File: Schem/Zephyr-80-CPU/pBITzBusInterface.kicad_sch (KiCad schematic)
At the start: 1 part, among them J1 pBITzBus

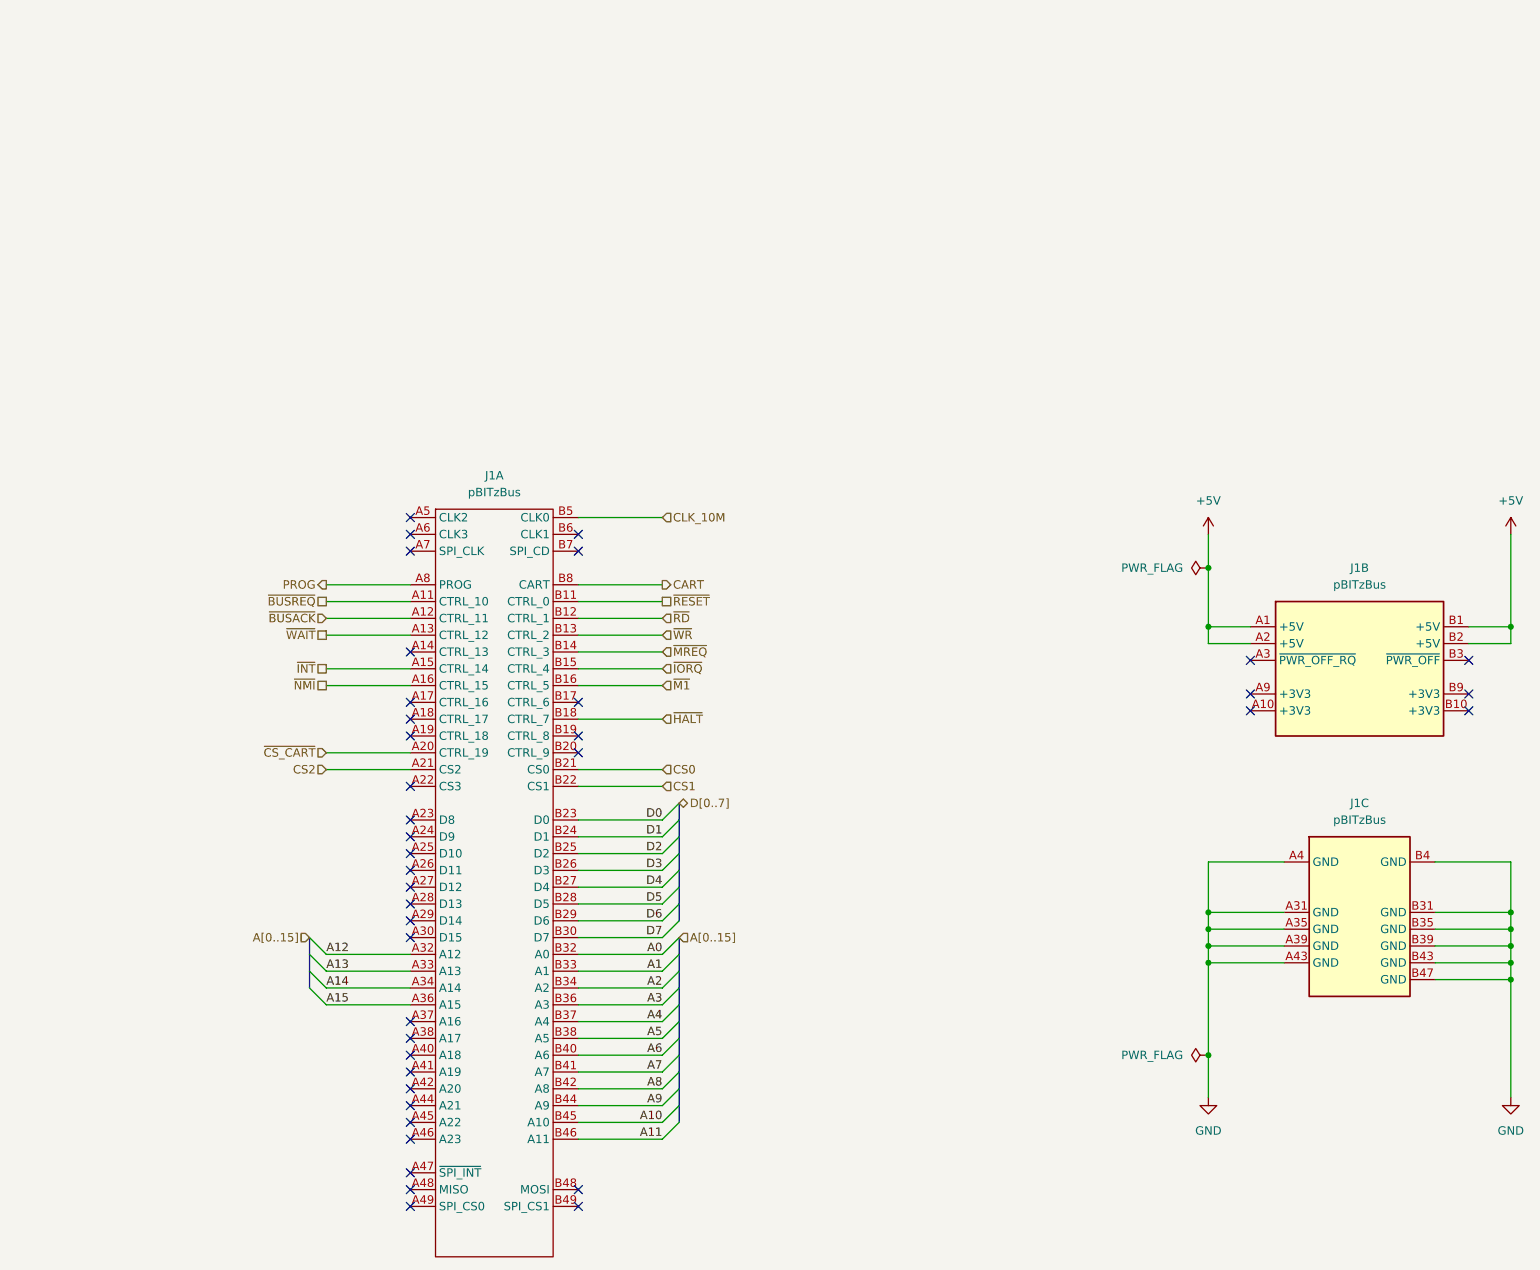
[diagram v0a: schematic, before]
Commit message: Moved to the DIN Connector
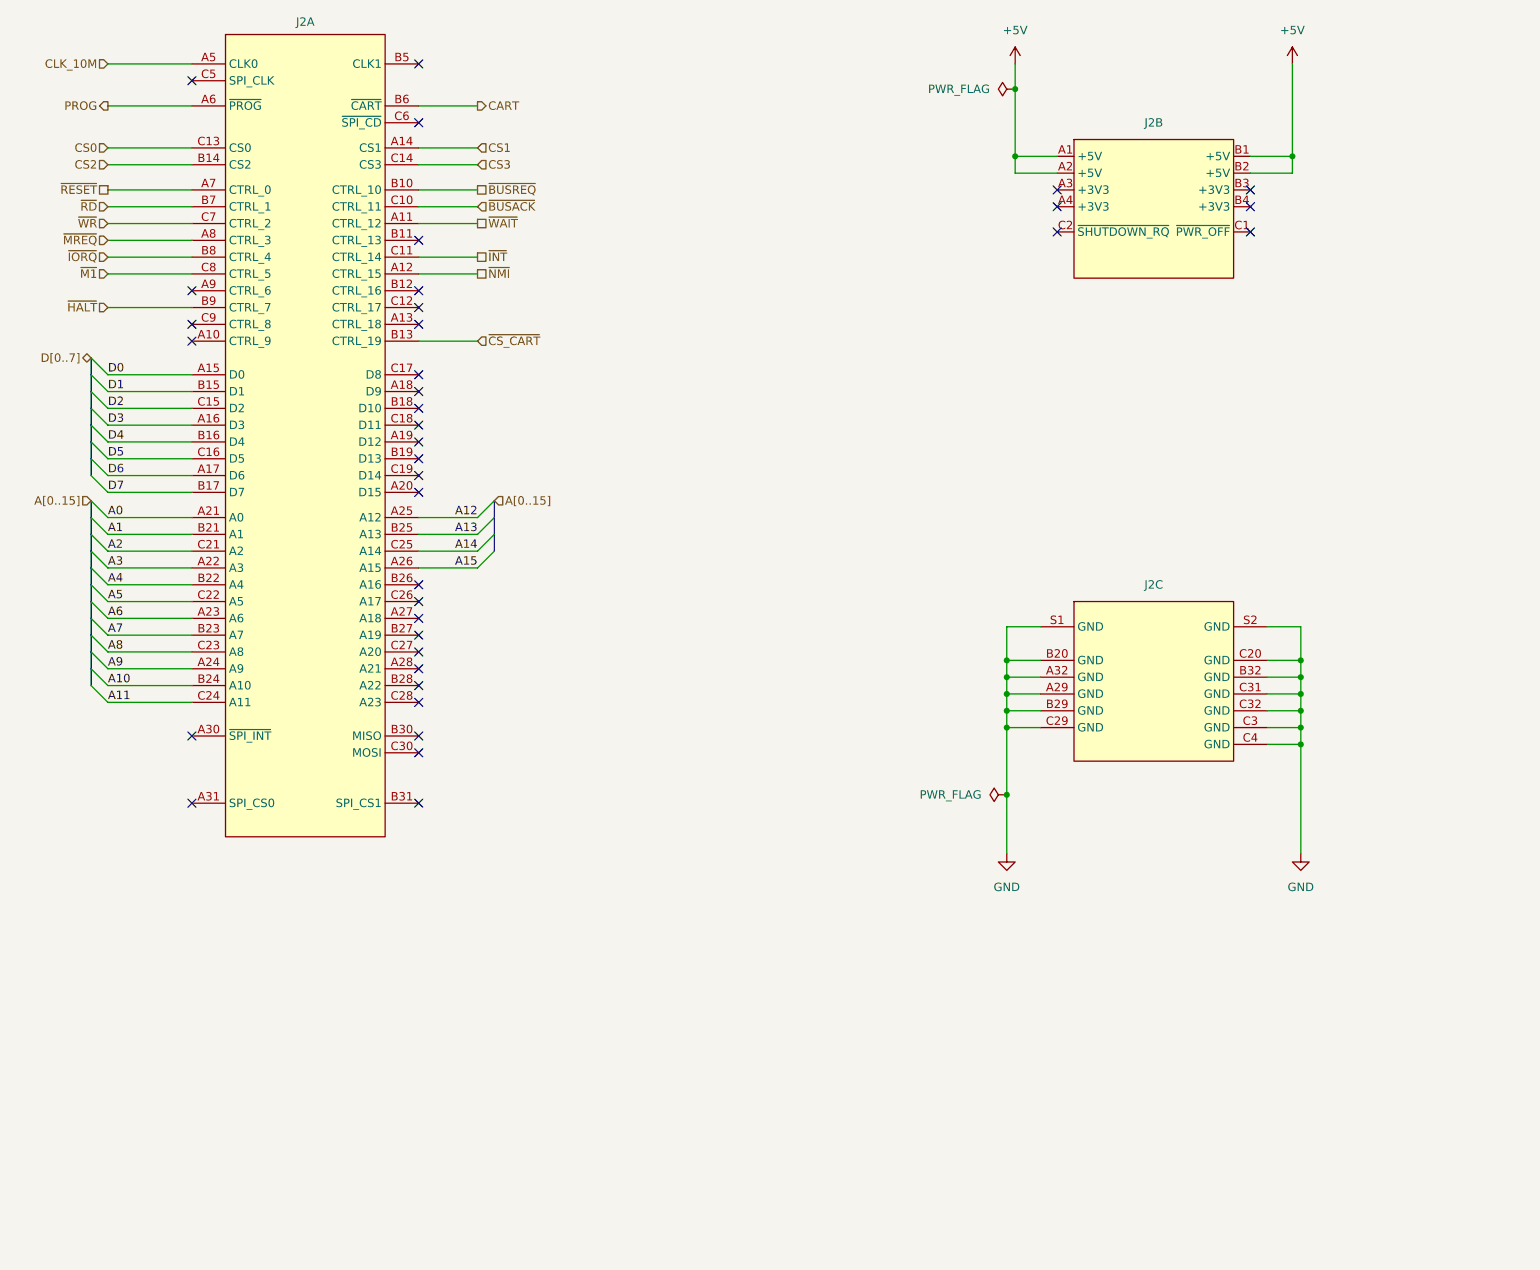
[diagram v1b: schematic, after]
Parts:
- removed J1: pBITzBus, Connector_PCBEdge:BUS_PCIexpress_x8, symbol pBITz:pBITzBus
- added J2: (no value), Footprints:AMPHENOL_86093967113T55F1LF, symbol pBITz:pBITzBus_DIN
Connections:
- net +5V: now also J2.A1 (+5V), J2.A2 (+5V), J2.B1 (+5V), J2.B2 (+5V)
- net A0: now also J2.A21 (A0)
- net A1: now also J2.B21 (A1)
- net A10: now also J2.B24 (A10)
- net A11: now also J2.C24 (A11)
- net A12: now also J2.A25 (A12)
- net A13: now also J2.B25 (A13)
- net A14: now also J2.C25 (A14)
- net A15: now also J2.A26 (A15)
- net A2: now also J2.C21 (A2)
- net A3: now also J2.A22 (A3)
- net A4: now also J2.B22 (A4)
- net A5: now also J2.C22 (A5)
- net A6: now also J2.A23 (A6)
- net A7: now also J2.B23 (A7)
- net A8: now also J2.C23 (A8)
- net A9: now also J2.A24 (A9)
- net CART: now also J2.B6 (~{CART})
- net CLK_10M: now also J2.A5 (CLK0)
- net CS0: now also J2.C13 (CS0)
- net CS1: now also J2.A14 (CS1)
- net CS2: now also J2.B14 (CS2)
- net D0: now also J2.A15 (D0)
- net D1: now also J2.B15 (D1)
- net D2: now also J2.C15 (D2)
- net D3: now also J2.A16 (D3)
- net D4: now also J2.B16 (D4)
- net D5: now also J2.C16 (D5)
- net D6: now also J2.A17 (D6)
- net D7: now also J2.B17 (D7)
- net GND: now also J2.A29 (GND), J2.A32 (GND), J2.B20 (GND), J2.B29 (GND), J2.B32 (GND), J2.C20 (GND), J2.C29 (GND), J2.C3 (GND), J2.C31 (GND), J2.C32 (GND), J2.C4 (GND), J2.S1 (GND), J2.S2 (GND)
- net PROG: now also J2.A6 (~{PROG})
- net ~{BUSACK}: now also J2.C10 (CTRL_11)
- net ~{BUSREQ}: now also J2.B10 (CTRL_10)
- net ~{CS_CART}: now also J2.B13 (CTRL_19)
- net ~{HALT}: now also J2.B9 (CTRL_7)
- net ~{INT}: now also J2.C11 (CTRL_14)
- net ~{IORQ}: now also J2.B8 (CTRL_4)
- net ~{M1}: now also J2.C8 (CTRL_5)
- net ~{MREQ}: now also J2.A8 (CTRL_3)
- net ~{NMI}: now also J2.A12 (CTRL_15)
- net ~{RD}: now also J2.B7 (CTRL_1)
- net ~{RESET}: now also J2.A7 (CTRL_0)
- net ~{WAIT}: now also J2.A11 (CTRL_12)
- net ~{WR}: now also J2.C7 (CTRL_2)
- new net CS3: J2.C14 (CS3)
- no-connect marks 40 -> 37

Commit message: updated parts #s
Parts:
- J2: MANUFACTURER_PART_NUMBER (none) -> 86093967113T55F1LF
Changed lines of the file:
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@@
+			)
+		)
+		(property "MANUFACTURER_PART_NUMBER" "86093967113T55F1LF"
+			(at 220.345 135.89 0)
+			(hide yes)
+			(show_name no)
+			(do_not_autoplace no)
+			(effects
+				(font
+					(size 1.27 1.27)
+				)
 			)
 		)
@@
 			)
 		)
+		(property "MANUFACTURER_PART_NUMBER" "86093967113T55F1LF"
+			(at 220.345 67.31 0)
+			(hide yes)
+			(show_name no)
+			(do_not_autoplace no)
+			(effects
+				(font
+					(size 1.27 1.27)
+				)
+			)
+		)
 		(pin "S2"
 		)
@@
 			(at 92.075 50.8 0)
 			(hide yes)
+			(show_name no)
+			(do_not_autoplace no)
+			(effects
+				(font
+					(size 1.27 1.27)
+				)
+			)
+		)
+		(property "MANUFACTURER_PART_NUMBER" "86093967113T55F1LF"
+			(at 92.075 50.8 0)
+			(hide yes)
